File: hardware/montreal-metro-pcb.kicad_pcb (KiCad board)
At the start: 2 copper layers, 160 x 160 mm, 95 parts, among them SW1 TS-1187A-B-A-B, SW2 TS-1187A-B-A-B, SW3 TS-1187A-B-A-B, SW4 TS-1187A-B-A-B, U1 XIAO-RP2040-DIP

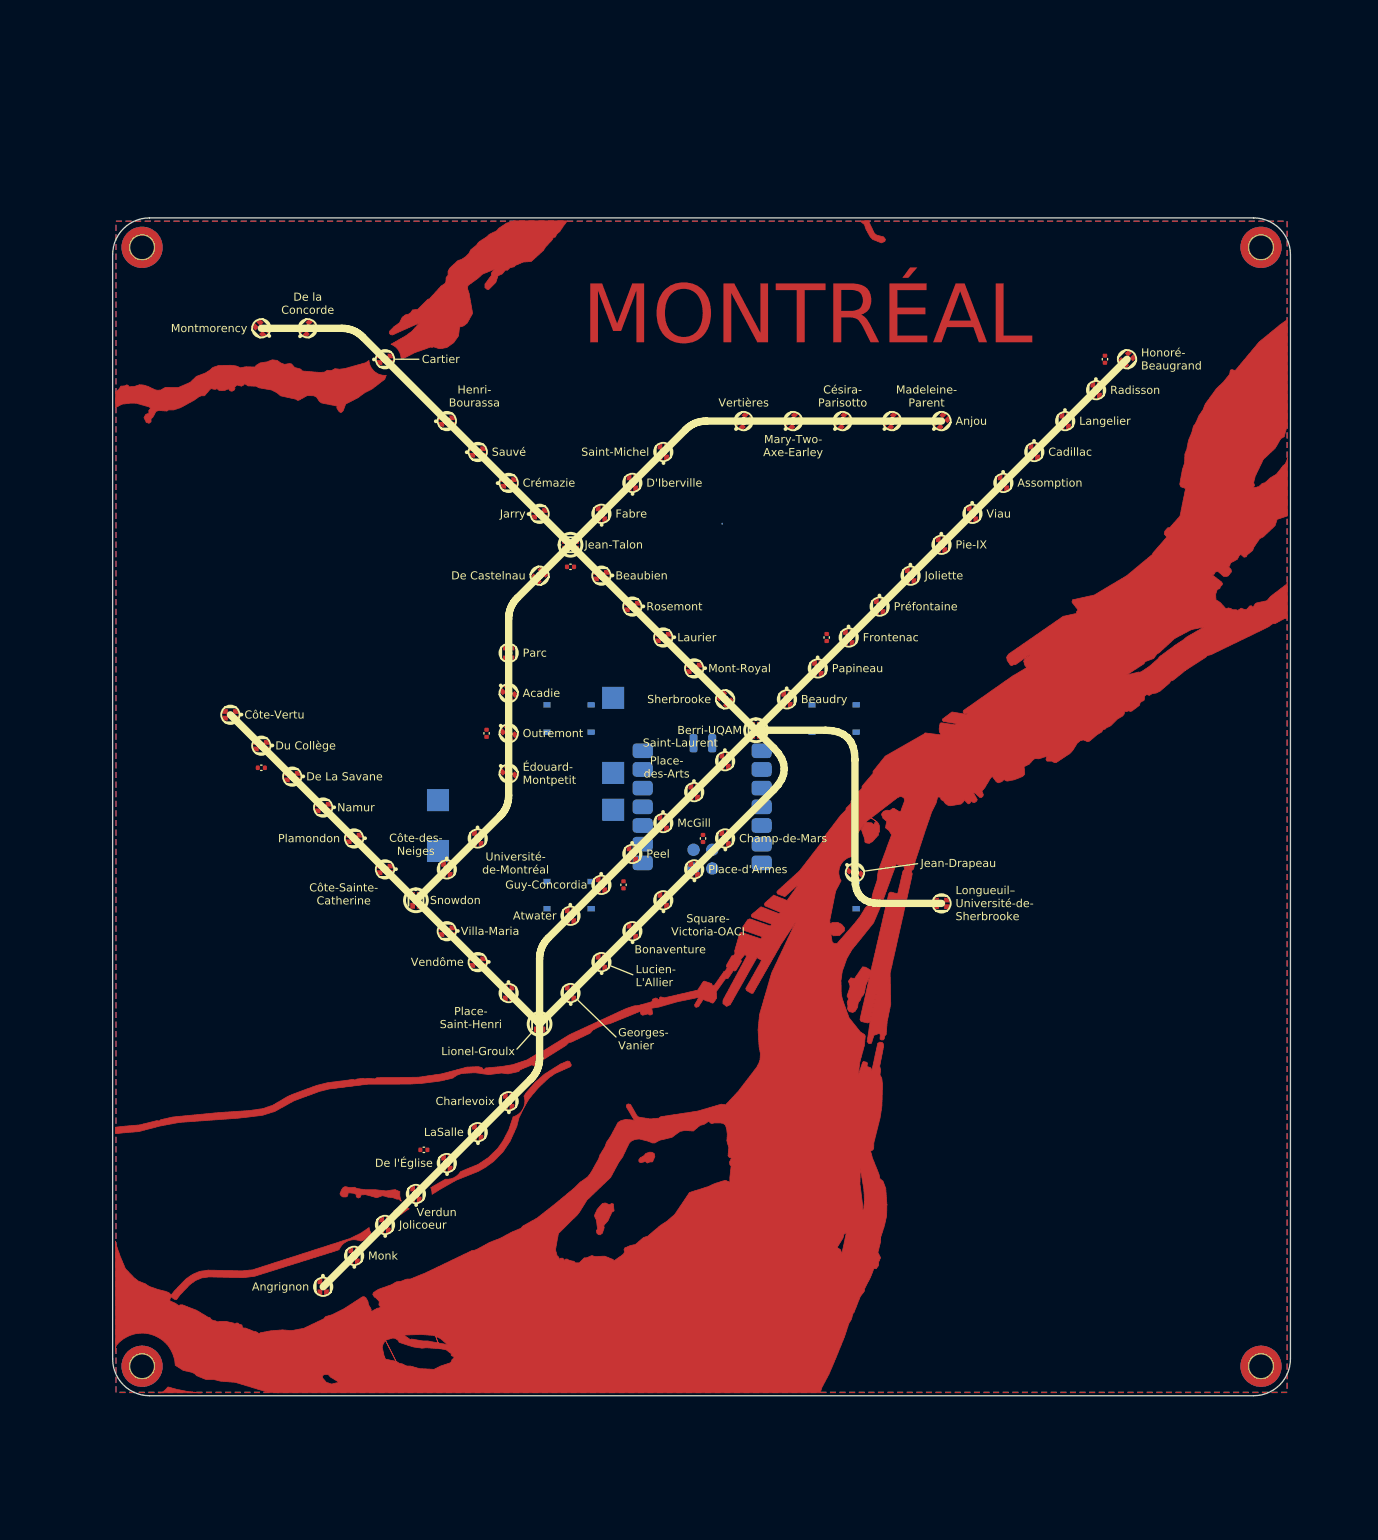
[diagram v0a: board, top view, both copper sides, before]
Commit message: Autoroute the board with Freerouting; DRC clean
tools/autoroute.py exports a Specctra file from a throwaway copy of the
board with track-and-via keepouts over the bare-copper front artwork
(islands kept open), and with the ground plane declared on the back only so
every front ground pad gets a via. It imports the routed session back.
tools/stitch_ground.py ties U1's ground pad into the back pour.

To make the board routable:
- stations that touch water get a 3.4 mm clearing so vias fit beside them
- the XIAO and buttons move to (124, 122) mm on the back, away from the
  downtown LEDs; the three test points move to a row below them
- +5V gets a 0.5 mm net class

Result: 944 track segments, 82 vias; 0 DRC violations, 0 unconnected
items, 0 schematic parity issues.

Co-Authored-By: Claude Opus 5.5 <noreply@anthropic.com>
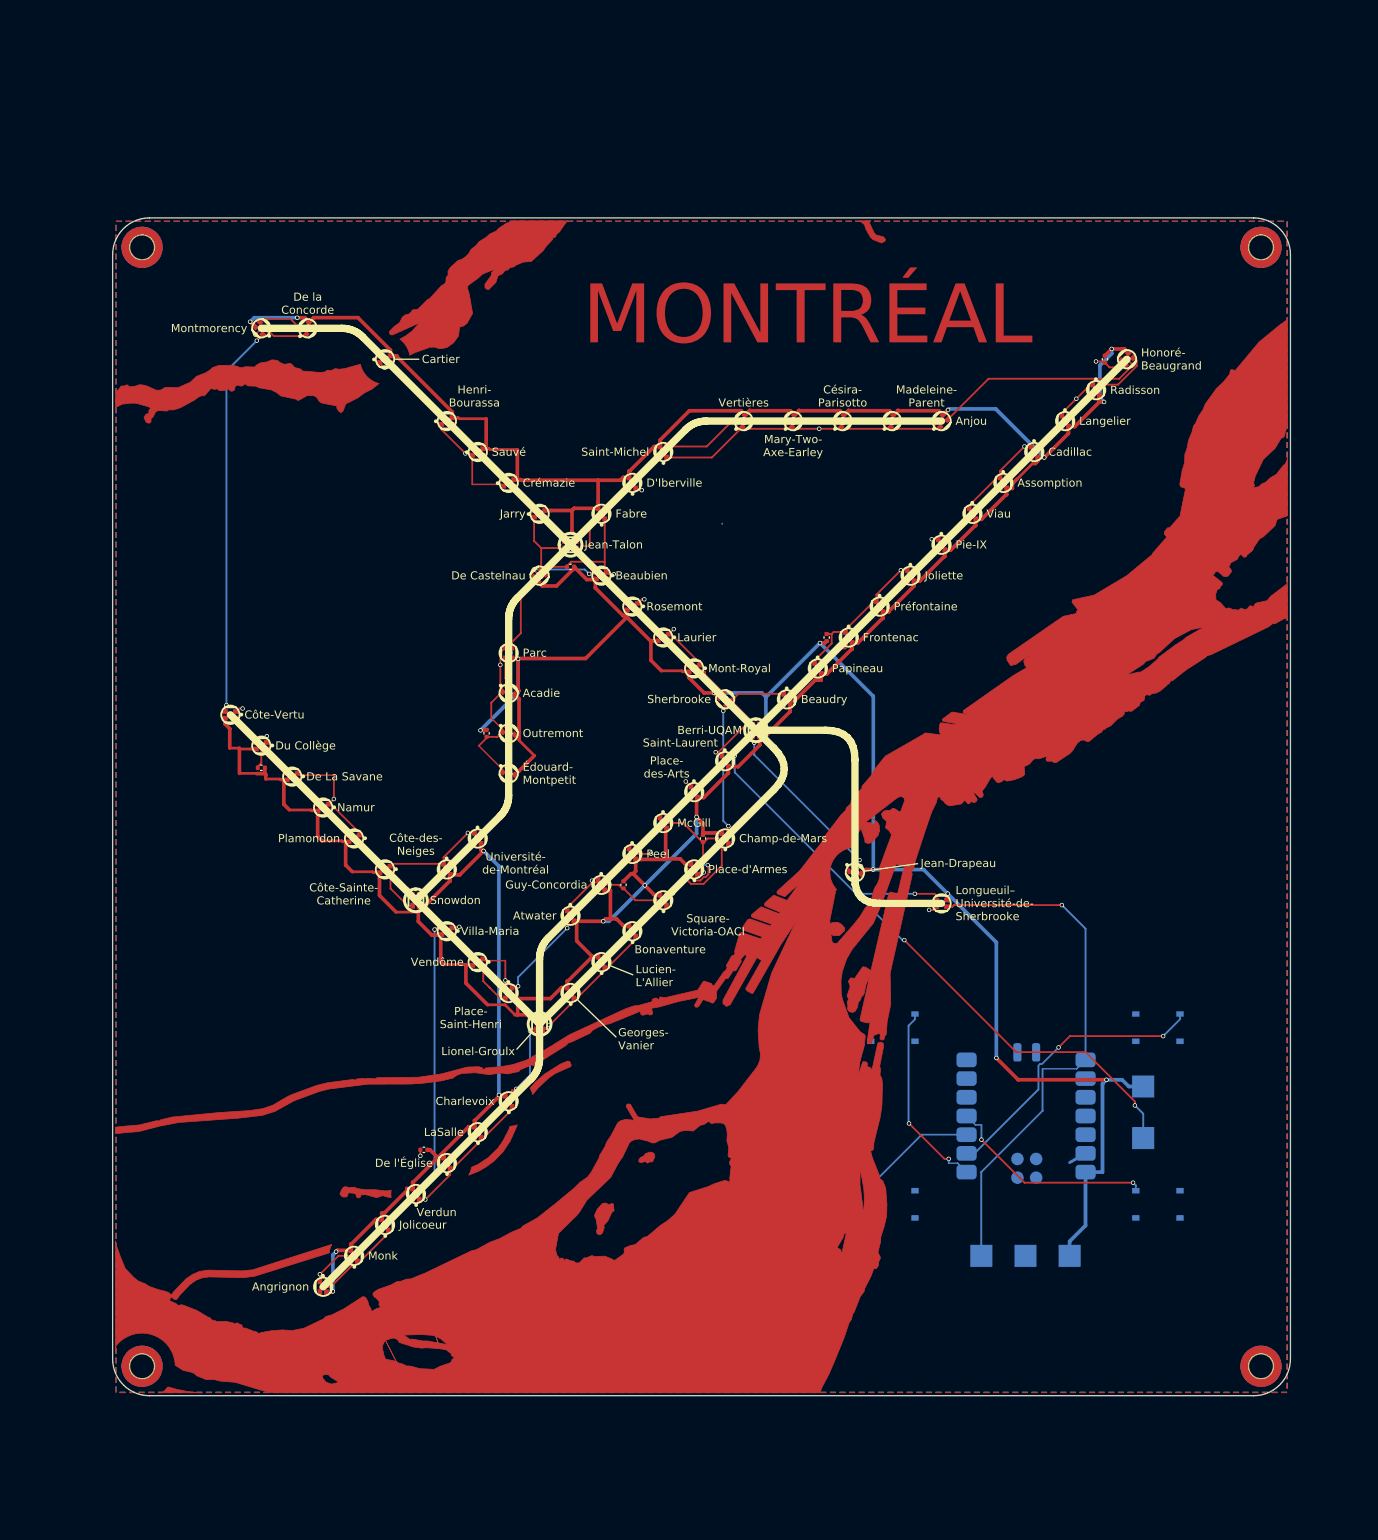
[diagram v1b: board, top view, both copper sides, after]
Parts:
- moved LED_OUT1 103.4 mm to (140.0, 125.0)
- moved +5V1 103.4 mm to (140.0, 118.0)
- moved LED_IN1 90.8 mm to (118.0, 141.0)
- moved +5V2 86.7 mm to (130.0, 141.0)
- moved GND1 86.3 mm to (124.0, 141.0)
- moved SW1 60.8 mm to (106.0, 110.0)
- moved SW2 60.8 mm to (106.0, 134.0)
- moved SW3 60.8 mm to (142.0, 110.0)
- moved SW4 60.8 mm to (142.0, 134.0)
- moved U1 60.8 mm to (124.0, 122.0)
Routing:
- net +5V: track 0.00 -> 737.4 mm, vias 0 -> 22
- net GND: track 0.00 -> 325.4 mm, vias 0 -> 32
- net LED_OUT: track 0.00 -> 81.4 mm, vias 0 -> 3
- net LED_IN: track 0.00 -> 73.3 mm, vias 0 -> 1
- net Net-(LED64-DO): track 0.00 -> 55.3 mm, vias 0 -> 2
- net Net-(LED31-DO): track 0.00 -> 53.3 mm, vias 0 -> 2
- net BUTTON_02: track 0.00 -> 39.2 mm, vias 0 -> 2
- net Net-(LED15-DO): track 0.00 -> 30.4 mm
- net BUTTON_04: track 0.00 -> 28.8 mm, vias 0 -> 2
- net BUTTON_01: track 0.00 -> 26.1 mm, vias 0 -> 2
- net Net-(LED2-DO): track 0.00 -> 24.1 mm, vias 0 -> 2
- net ROW6: track 0.00 -> 17.8 mm, vias 0 -> 2
- net BUTTON_03: track 0.00 -> 16.6 mm
- net Net-(LED1-DO): track 0.00 -> 13.5 mm, vias 0 -> 2
- net Net-(LED51-DO): track 0.00 -> 12.6 mm
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
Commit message: Apply map markups: label position rule, hand placements, tidier water
Labels (tools/auto_label.py):
- rank positions by the cartographers' rule of thumb: upper right, lower
  right, upper left, lower left, middle right, middle left
- --fixed FILE: hand placements that are applied first and never moved
- --parallel: give a group of stations leaders at the same angle
- input/label_overrides-square.json: Cartier lower left, Verdun upper left

Water (input/build_schematic.py):
- drop pieces cut off by the board edge under 20 mm^2
- fill islands under 8 mm^2 or thinner than 0.8 mm
- drop canal stubs left beside stations by the pad clearings
- cut the water back under hand-placed labels

tools/rebuild_board.sh regenerates the board end to end. Board re-routed:
0 DRC violations, 0 unconnected, 0 parity issues.

Co-Authored-By: Claude Opus 5.5 <noreply@anthropic.com>
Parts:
- moved ROW6 6.38 mm to (48.4, 128.4), turned to 90 degrees
- moved ROW0 4.24 mm to (100.0, 60.0), turned to 0 degrees
- moved ROW1 4.24 mm to (137.8, 22.2), turned to 0 degrees
- moved ROW5 4.24 mm to (83.2, 87.3), turned to 0 degrees
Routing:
- net +5V: track 737.4 -> 755.9 mm, vias 22 -> 21
- net LED_OUT: track 81.4 -> 97.1 mm
- net Net-(LED51-DO): track 12.6 -> 4.83 mm
- net Net-(LED52-DO): track 11.8 -> 4.83 mm, vias 2 -> 0
- net GND: track 325.4 -> 321.4 mm
- net Net-(LED5-DO): track 4.84 -> 8.32 mm
- net Net-(LED15-DO): track 30.4 -> 27.2 mm, vias 0 -> 2
- net ROW6: track 17.8 -> 19.1 mm
- net Net-(LED14-DO): track 7.43 -> 8.50 mm

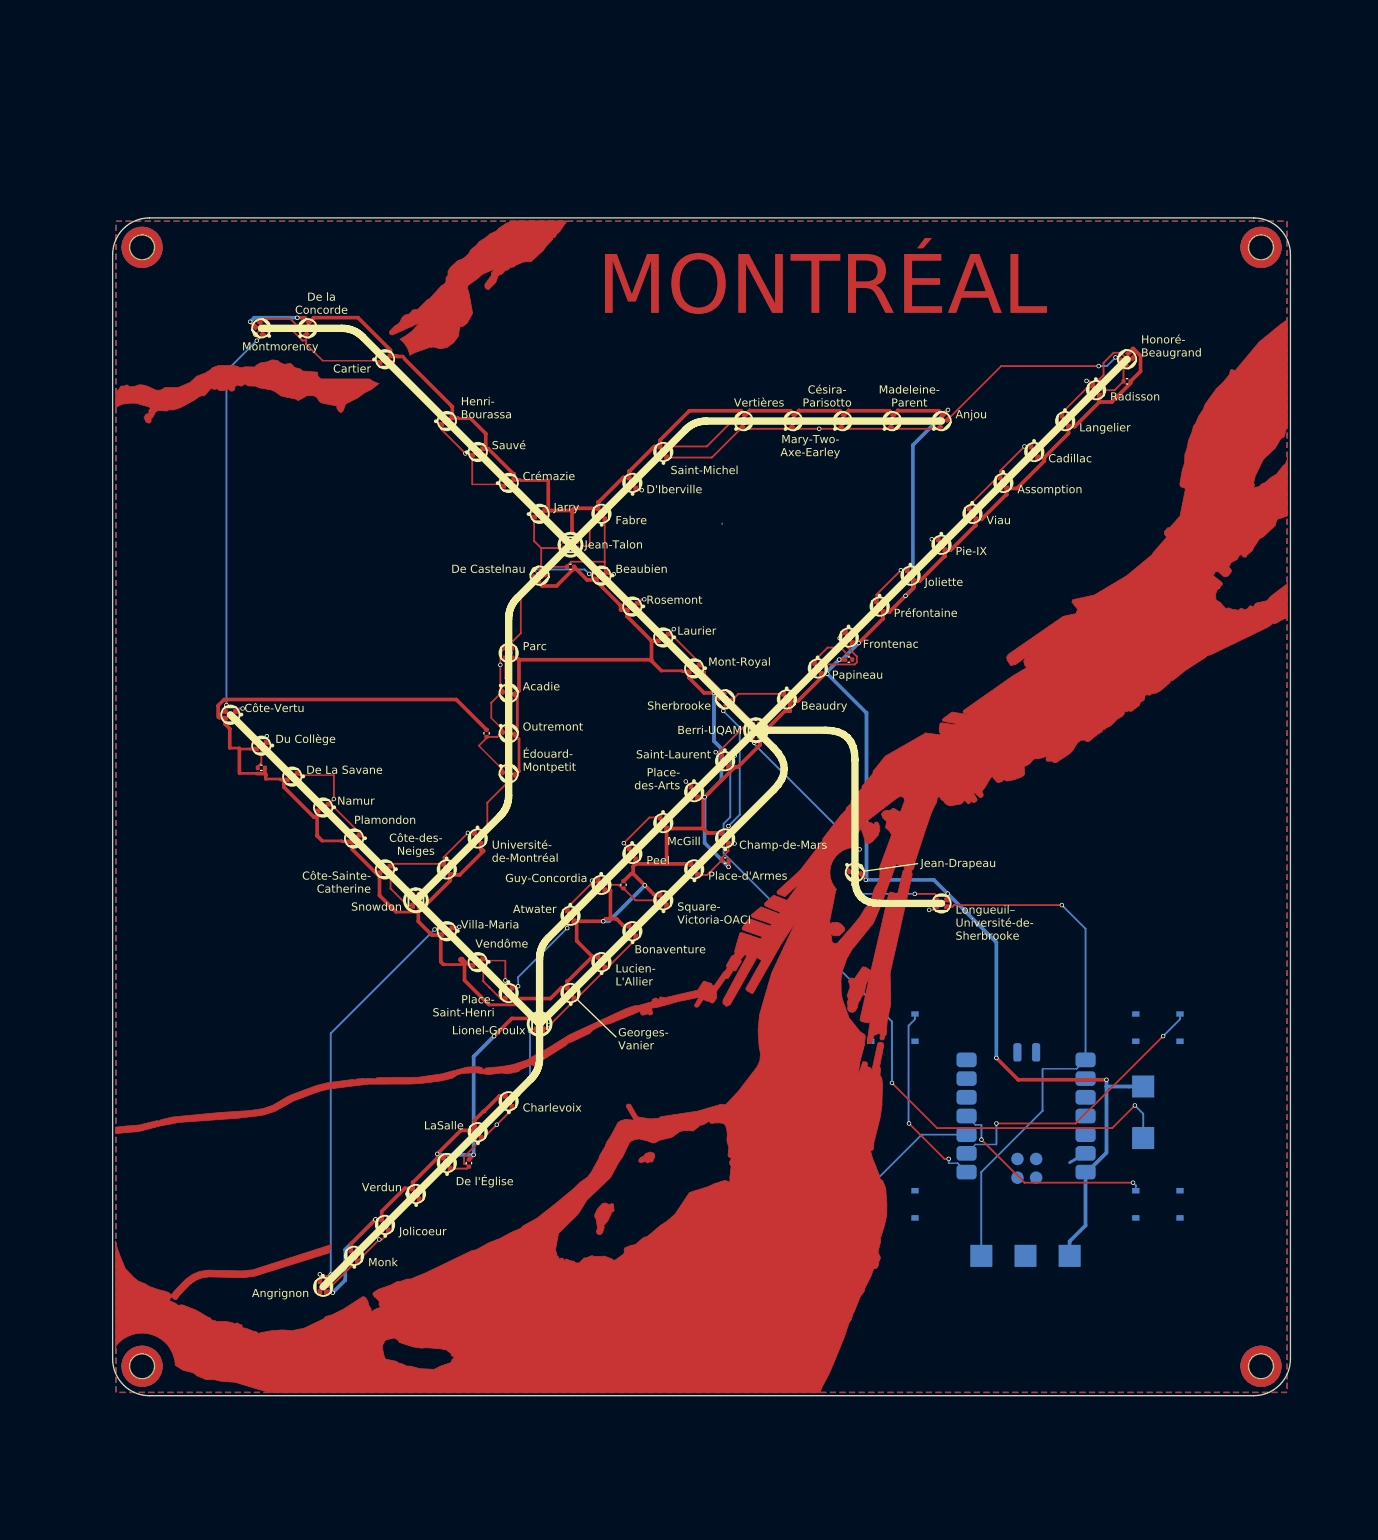
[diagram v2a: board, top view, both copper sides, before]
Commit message: Import the hand label pass from KiCad and freeze it
41 of 73 station labels were moved, re-wrapped or retyped by hand in KiCad.
import_labels.py brought them into montreal-schematic-square.json; they are
now frozen in input/label_overrides-square.json ({station: {label, wrap}}).

- build_schematic.py re-applies the overrides on every build and cuts the
  water back under each hand-placed label
- auto_label.py --fixed accepts the new format and never moves them
- tools/save_label_overrides.py freezes the labels of a data file
- check_fit: pad and line clearances calibrated to the hand pass
- hardware/backups/: the board as hand-edited, before any regeneration

The board file is committed as edited by hand; it has not been regenerated.

Co-Authored-By: Claude Opus 5.5 <noreply@anthropic.com>
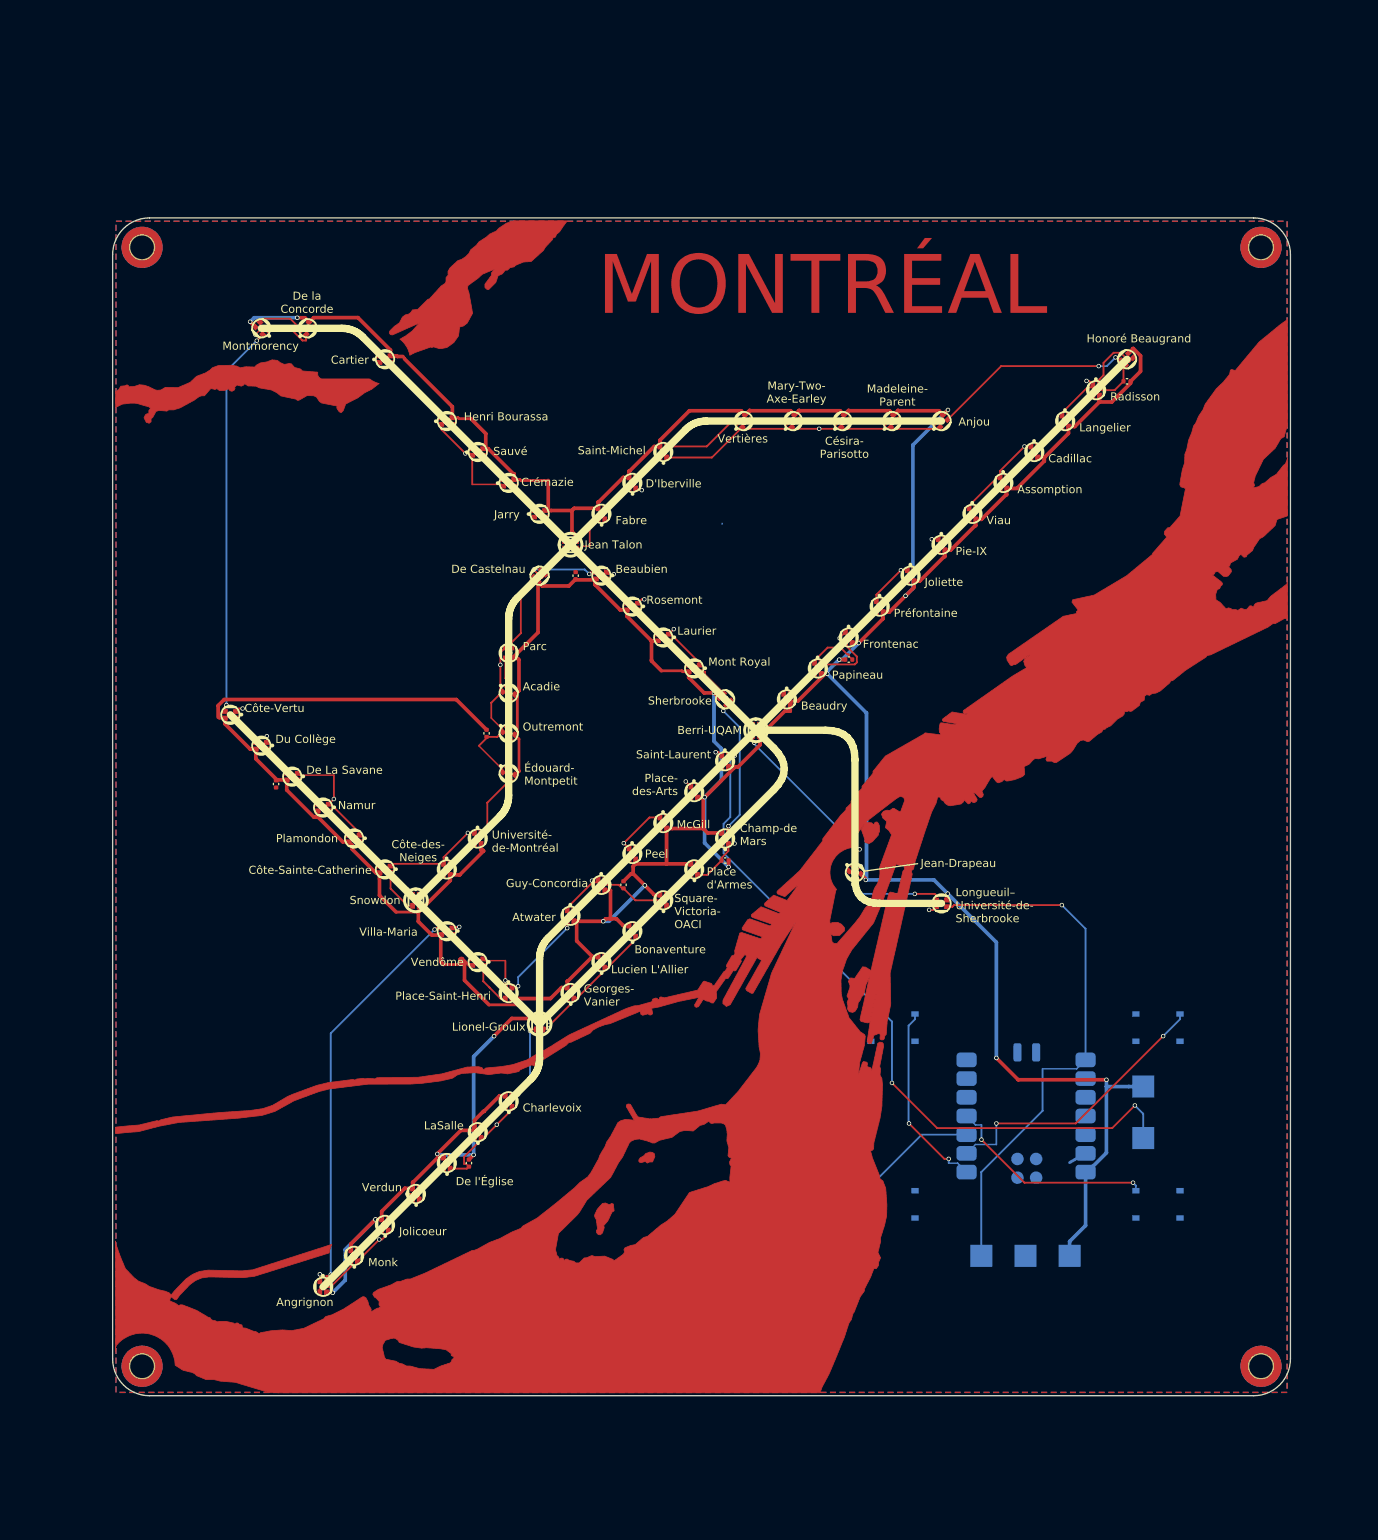
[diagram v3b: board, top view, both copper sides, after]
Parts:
- moved ROW3 2.97 mm to (22.2, 76.9), turned to 90 degrees
- moved ROW2 1.39 mm to (62.9, 48.6), turned to -90 degrees
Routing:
- net GND: track 321.4 -> 262.2 mm
- net +5V: track 755.9 -> 740.2 mm
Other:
- board text added: "Champ-de Mars"
- board text added: "Côte-Sainte-Catherine"
- board text added: "Henri Bourassa"
- board text added: "Honoré Beaugrand"
- board text added: "Jean Talon"
- board text added: "Lucien L'Allier"
- board text added: "Mont Royal"
- board text added: "Place d'Armes"
- board text added: "Place-Saint-Henri"
- board text added: "Square- Victoria- OACI"
- board text removed: "Champ-de-Mars"
- board text removed: "Côte-Sainte- Catherine"
- board text removed: "Henri- Bourassa"
- board text removed: "Honoré- Beaugrand"
- board text removed: "Jean-Talon"
- board text removed: "Lucien- L'Allier"
- board text removed: "Mont-Royal"
- board text removed: "Place- Saint-Henri"
- board text removed: "Place-d'Armes"
- board text removed: "Square- Victoria-OACI"
